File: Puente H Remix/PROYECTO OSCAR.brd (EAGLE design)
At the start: 27.7 x 27.3 mm, 11 parts, among them IC1 LM324D

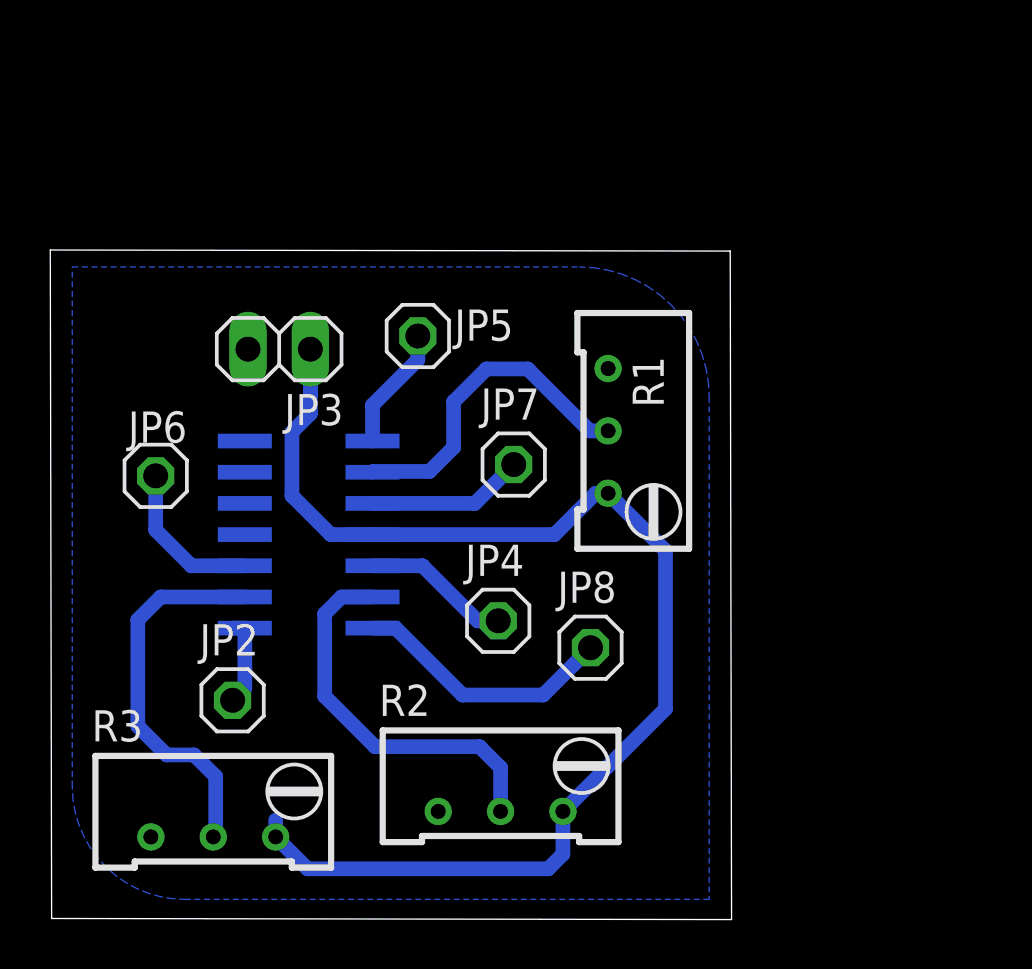
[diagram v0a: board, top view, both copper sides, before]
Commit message: Se agregan conexiones y archivos de configuración CNC
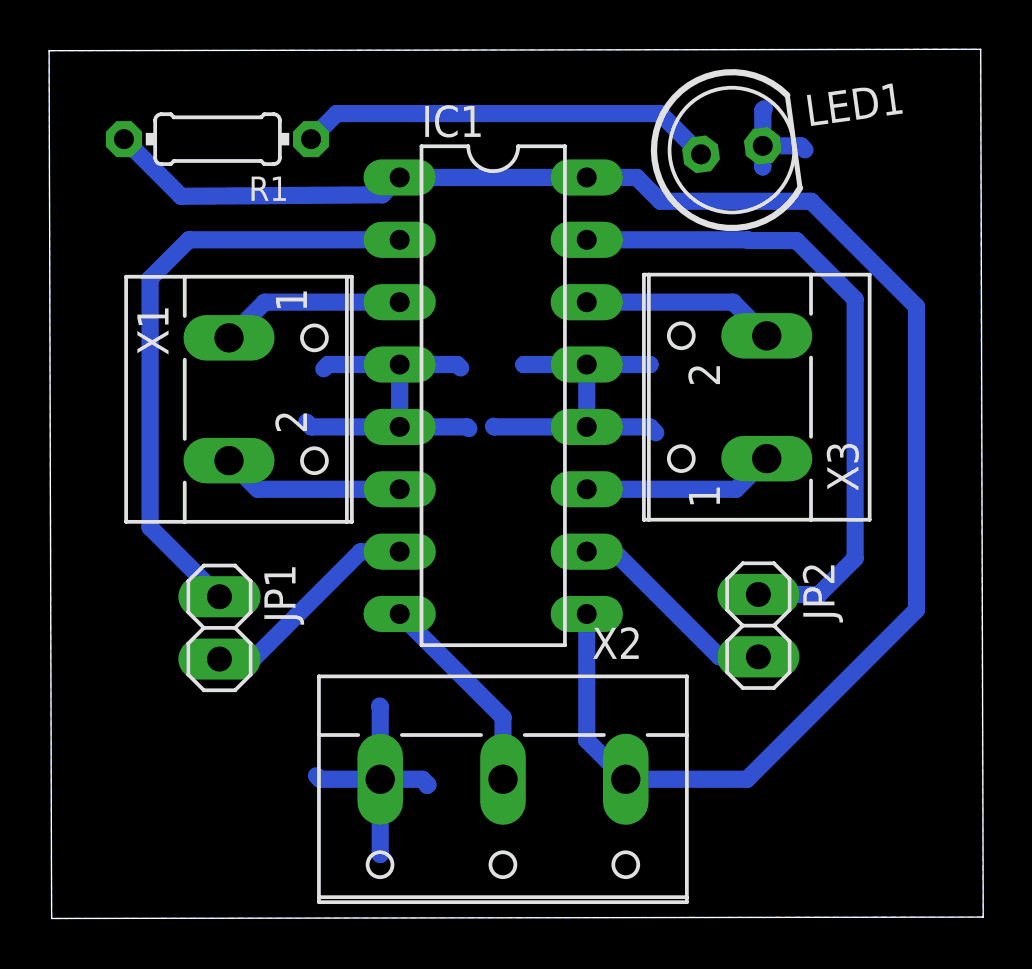
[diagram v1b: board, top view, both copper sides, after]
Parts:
- removed JP3: (no value), pinhead:1X02
- removed JP4, JP5, JP6, JP7, JP8: (no value), pinhead:1X01
- removed R2, R3: (no value), rcl:RTRIM64W
- added JP1: (no value), pinhead:1X02
- added LED1: (no value), led:LED5MM
- added X1, X3: (no value), con-wago-500:W237-102
- added X2: (no value), con-wago-500:W237-103
- IC1: value LM324D -> L293D; device linear:SO14 -> st-microelectronics:DIL16
- JP2: device pinhead:1X01 -> pinhead:1X02
- R1: device rcl:RTRIM64W -> rcl:0204/7
- moved JP2 21.6 mm to (28.8, 11.9), turned to 270 degrees
- moved R1 20.9 mm to (6.76, 31.7), turned to 0 degrees
- moved IC1 9.41 mm to (18.0, 21.3), flipped to the top
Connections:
- removed net BAND: IC1.10, JP6.1
- removed net CMPB: IC1.8, JP2.1
- removed net CMPH: IC1.7, JP8.1
- removed net CMPL: IC1.1, JP5.1
- removed net HIGH: IC1.5, JP4.1
- removed net LOW: IC1.3, JP7.1
- removed net N$16: IC1.9, R3.2
- new net BACK_L: IC1.7, JP1.2
- new net BACK_R: IC1.10, JP2.2
- new net FWD_L: IC1.2, JP1.1
- new net FWD_R: IC1.15, JP2.1
- new net N$2: IC1.3, X1.1
- new net N$4: IC1.14, X3.2
- new net N$5: IC1.11, X3.1
- new net VSS: IC1.8, X2.2
- net GND: now also IC1.12, IC1.13, IC1.4, IC1.5, LED1.K, X2.3; no longer IC1.11, JP3.2, R1.1, R2.1, R3.1
- net N$1: now also LED1.A; no longer IC1.2
- net N$3: now also X1.2; no longer R2.2
- net VCC: now also IC1.1, IC1.16, IC1.9, R1.1, X2.1; no longer IC1.4, JP3.1, R1.3, R2.3, R3.3
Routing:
- net GND: track 0.00 -> 44.4 mm
- net FWD_R: track 0.00 -> 27.0 mm
- net FWD_L: track 0.00 -> 24.9 mm
- net VCC: track 52.9 -> 70.2 mm
- net N$16: track 15.6 -> 0.00 mm
- net CMPH: track 10.8 -> 0.00 mm
- net BACK_L: track 0.00 -> 9.15 mm
- net BACK_R: track 0.00 -> 8.76 mm
- net VSS: track 0.00 -> 8.48 mm
- net N$3: track 15.7 -> 7.43 mm
- net N$4: track 0.00 -> 7.90 mm
- net N$5: track 0.00 -> 7.85 mm
- net N$2: track 0.00 -> 7.55 mm
- net BAND: track 6.45 -> 0.00 mm
- net LOW: track 6.41 -> 0.00 mm
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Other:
- board size 27.7 x 27.3 mm -> 38 x 35.4 mm
